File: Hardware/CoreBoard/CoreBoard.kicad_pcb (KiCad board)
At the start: 2 copper layers, 135.1 x 84.3 mm, 92 parts, among them J1 RJ45_LED_Shielded, SW1 SW_Push, SW10 SW_Push, SW11 SW_Push, SW12 SW_Push, SW13 SW_Push, SW14 SW_Push, SW15 SW_Push, SW16 SW_SPDT, SW2 SW_Push, SW3 SW_Push, SW4 SW_Push, SW5 SW_Push, SW6 SW_Push, SW7 SW_Push, SW8 SW_Push, SW9 SW_Push, U1 Teensy4.1_DEV-16771, U3 SHHD003A0A, U4 74HC148, U5 74HC148, U6 74HC00, U7 OKI

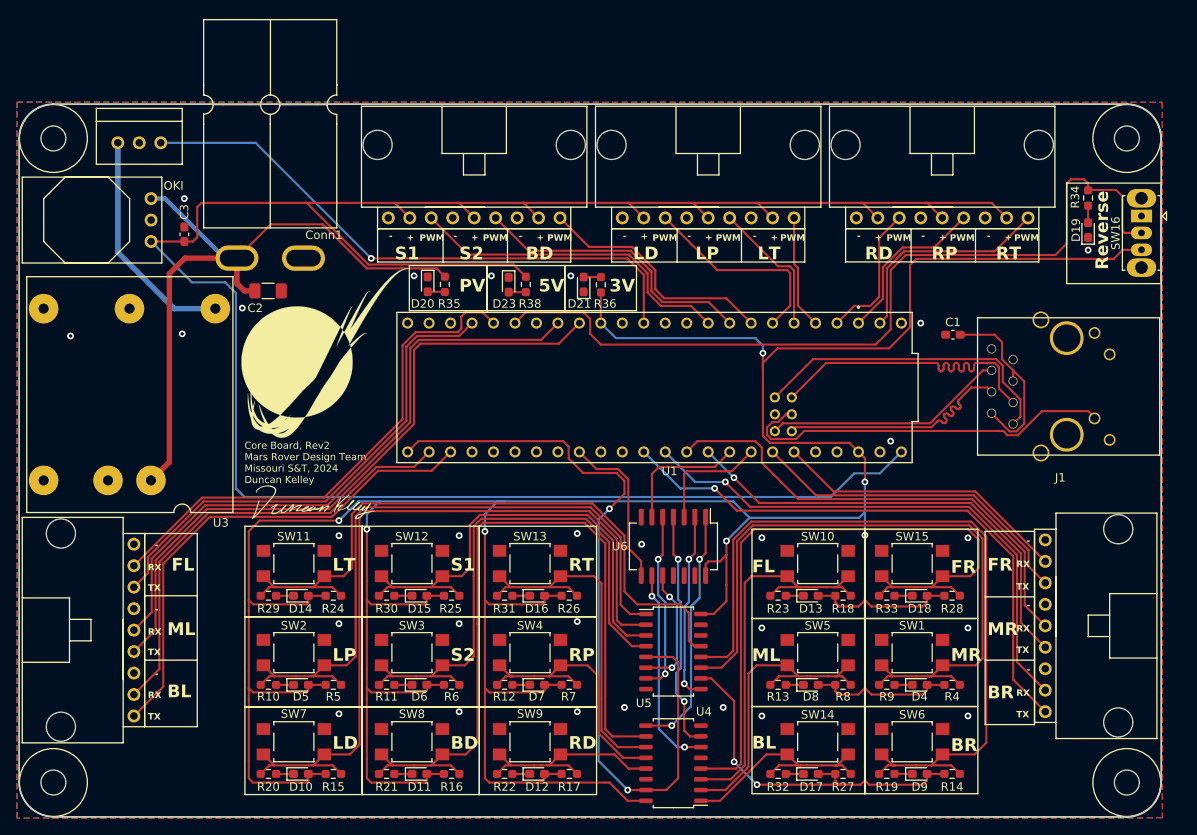
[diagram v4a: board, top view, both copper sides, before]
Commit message: added accelerometer and touch-ups
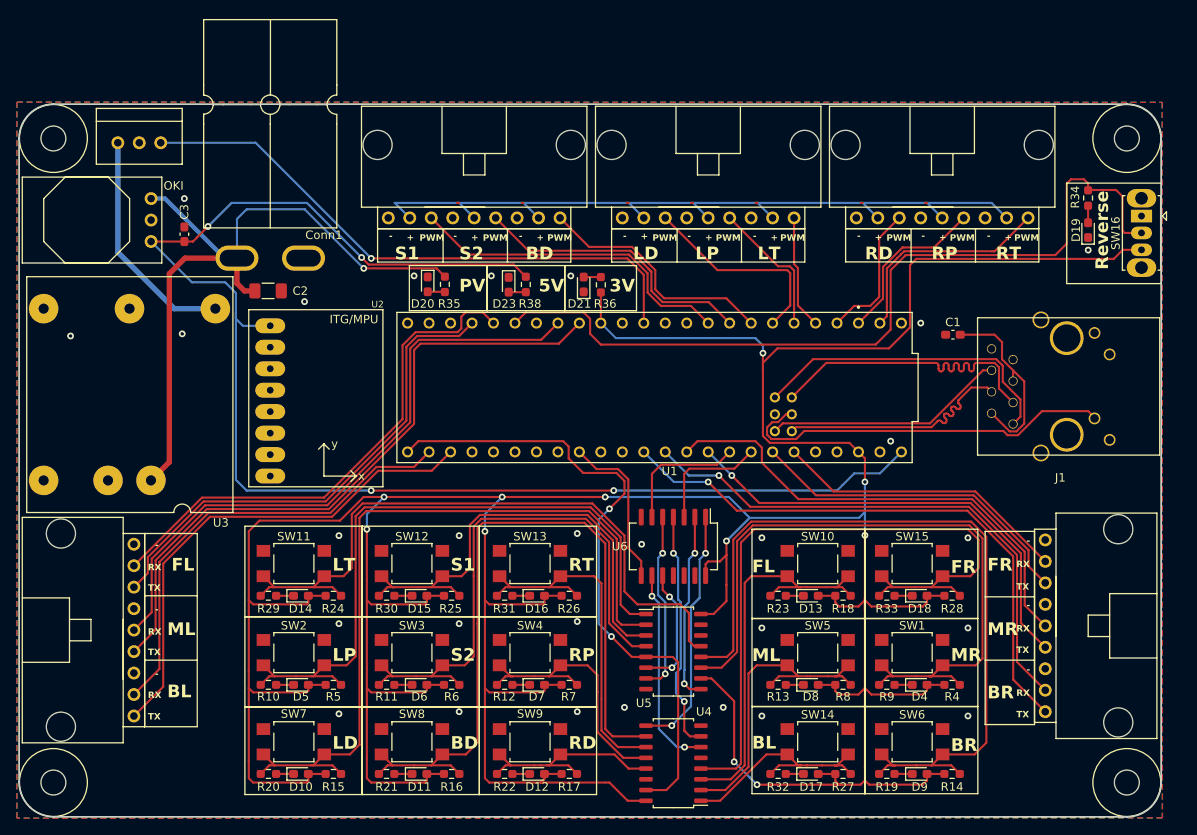
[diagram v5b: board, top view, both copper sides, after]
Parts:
- added U2: GY-521, GY-521:GY-521, F.Cu at (103.4, 77.5)
- G*** (x2): moved to B.Cu
- moved G*** 81.3 mm to (175.3, 119.1), turned to 180 degrees
- moved G*** 77.2 mm to (173.2, 99.3), turned to 180 degrees
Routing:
- net Out3: track 92.5 -> 76.5 mm
- net +5V: track 274.7 -> 265.9 mm, vias 0 -> 4
- net PV: track 81.5 -> 85.7 mm, vias 0 -> 1
- net +3V3: track 517.1 -> 518.2 mm, vias 9 -> 11
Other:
- board text added: "Riley Shoop-Altom"

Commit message: finished adding accelerometer
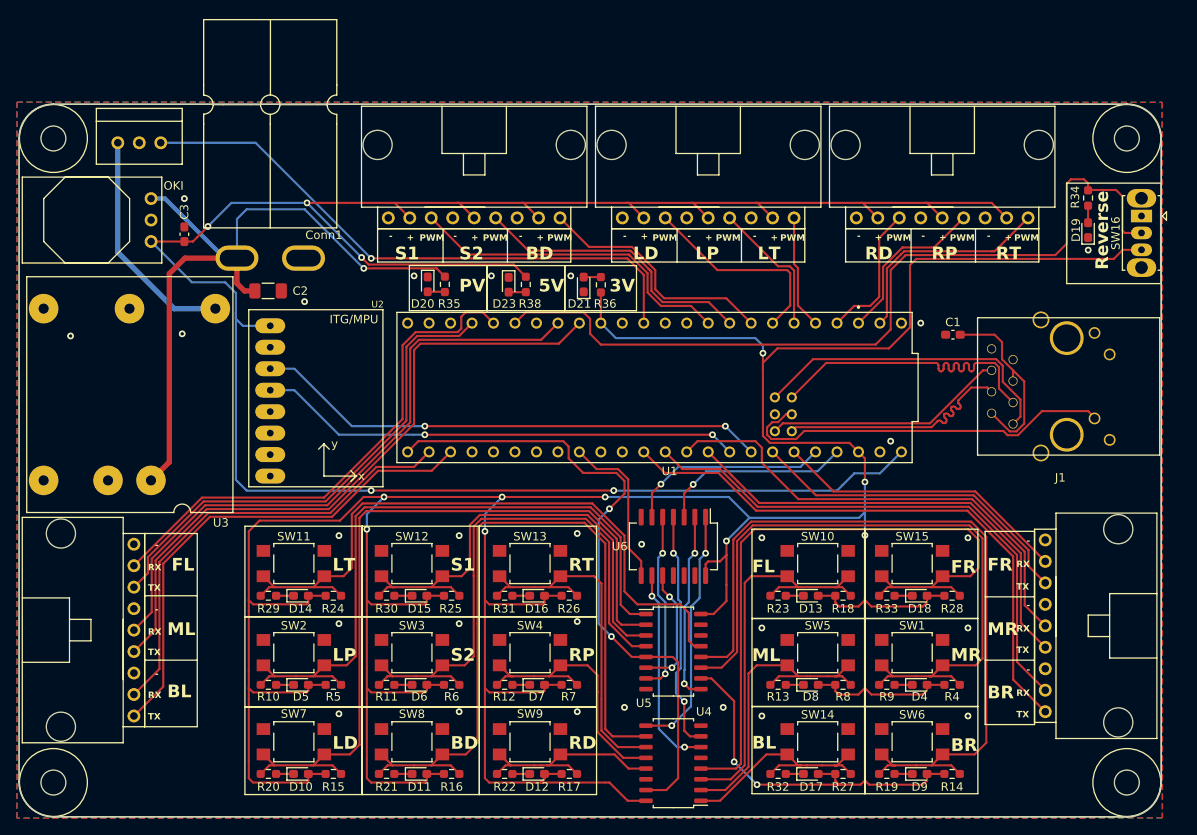
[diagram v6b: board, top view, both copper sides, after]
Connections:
- U1 pad 18: Out1 -> AccSDA
- U1 pad 19: Out0 -> AccSCL
- U1 pad 22: unconnected-(U1-A8-Pad22) -> Out1
- U1 pad 23: unconnected-(U1-A9-Pad23) -> Out0
- U2 pad ADO: unconnected-(U2-PadADO) -> GND
- U2 pad SCL: unconnected-(U2-PadSCL) -> AccSCL
- U2 pad SDA: unconnected-(U2-PadSDA) -> AccSDA
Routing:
- net AccSCL: track 0.00 -> 61.0 mm, vias 0 -> 2
- net AccSDA: track 0.00 -> 57.4 mm, vias 0 -> 2
- net +5V: track 265.9 -> 276.2 mm, vias 4 -> 5
- net Out1: track 15.4 -> 24.2 mm, vias 0 -> 1
- net Out0: track 14.1 -> 22.9 mm, vias 0 -> 1
- net BR_TX: vias 1 -> 0
- net MR_TX: vias 1 -> 0
- net BR_RX: vias 1 -> 0
